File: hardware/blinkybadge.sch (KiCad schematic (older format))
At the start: 13 parts

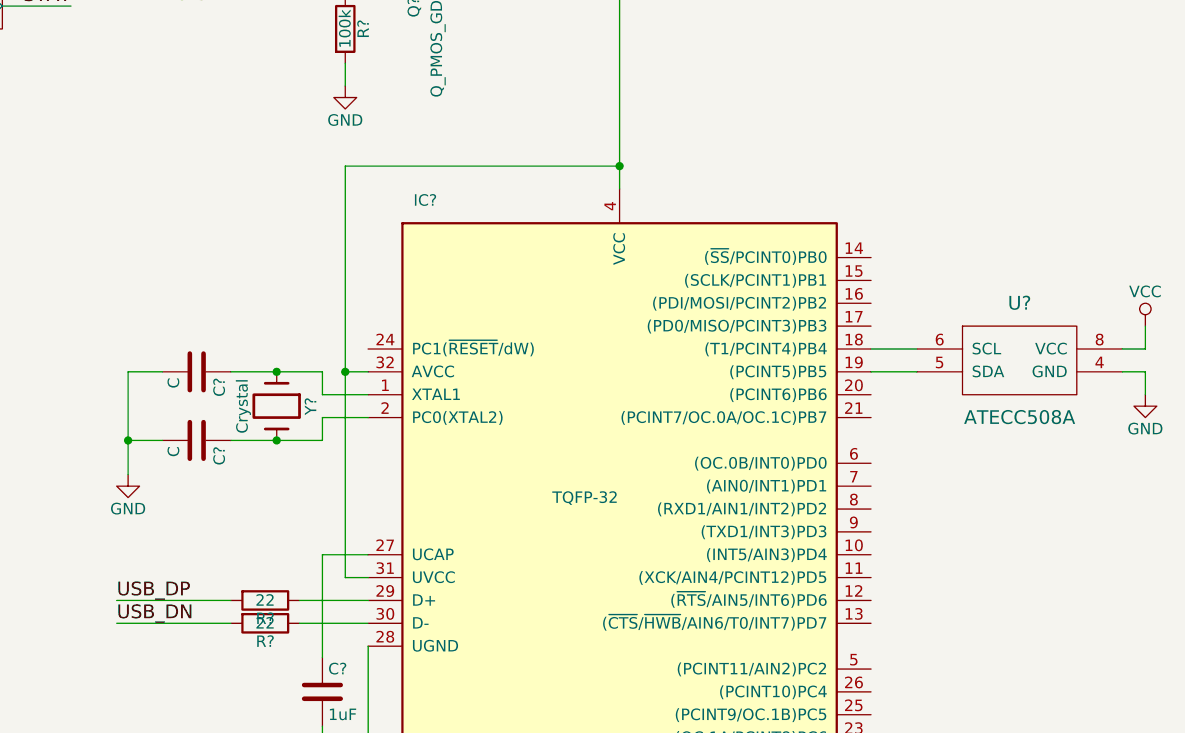
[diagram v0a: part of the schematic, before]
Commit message: Add LEDs
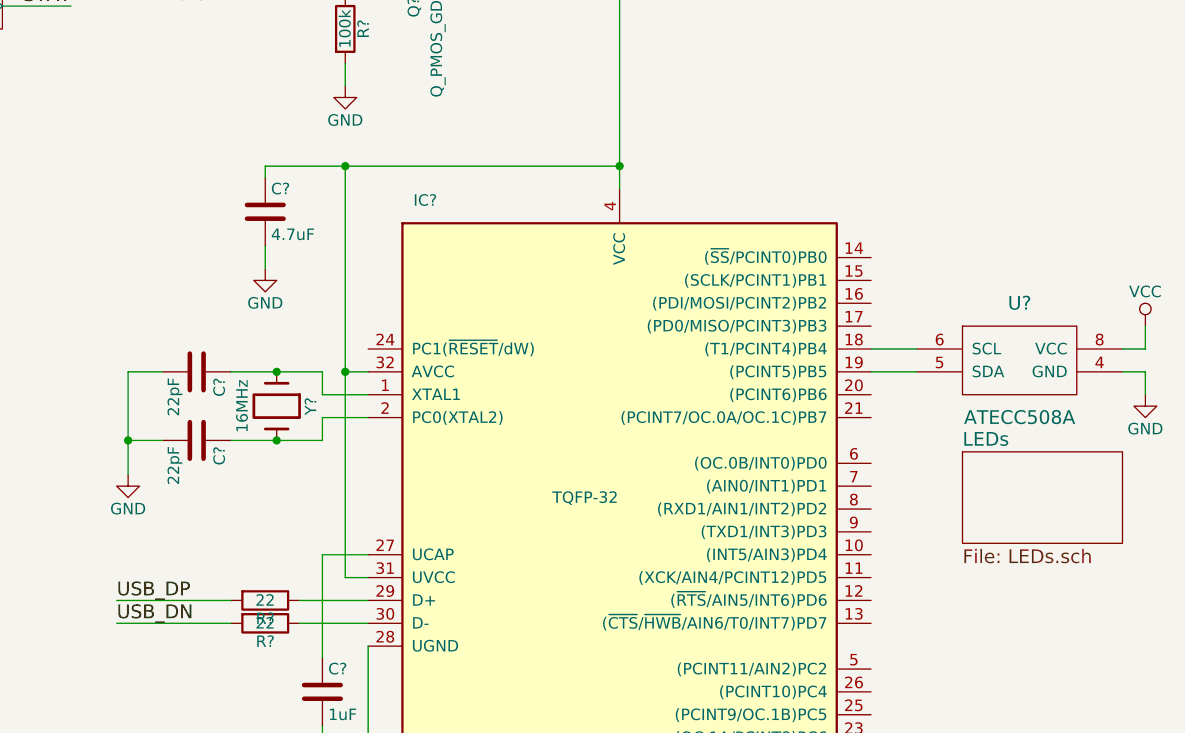
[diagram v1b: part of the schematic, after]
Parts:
- added C?: 4.7uF, symbol C
- C? (x2): value C -> 22pF
- Y?: value Crystal -> 16MHz
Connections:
- net GND: now also C?.2
- net VCC: now also C?.1
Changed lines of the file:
@@
 $Descr USLetter 11000 8500
 encoding utf-8
-Sheet 1 2
+Sheet 1 3
 Title "Crypto and Privacy Village 2016 Badge"
 Date ""
@@
 P 4200 3900
 F 0 "Y?" H 4200 4050 50  0000 C CNN
-F 1 "Crystal" H 4200 3750 50  0000 C CNN
+F 1 "16MHz" H 4200 3750 50  0000 C CNN
 F 2 "" H 4200 3900 50  0000 C CNN
 F 3 "" H 4200 3900 50  0000 C CNN
@@
 P 3850 3750
 F 0 "C?" H 3875 3850 50  0000 L CNN
-F 1 "C" H 3875 3650 50  0000 L CNN
+F 1 "22pF" H 3875 3650 50  0000 L CNN
 F 2 "" H 3888 3600 50  0000 C CNN
 F 3 "" H 3850 3750 50  0000 C CNN
@@
 P 3850 4050
 F 0 "C?" H 3875 4150 50  0000 L CNN
-F 1 "C" H 3875 3950 50  0000 L CNN
+F 1 "22pF" H 3875 3950 50  0000 L CNN
 F 2 "" H 3888 3900 50  0000 C CNN
 F 3 "" H 3850 4050 50  0000 C CNN
@@
 	8000 3650 8000 3550
 Wire Wire Line
-	5700 2850 4500 2850
+	4150 2850 5700 2850
 Wire Wire Line
 	4500 2850 4500 4650
@@
 	4500 4650 4600 4650
 Connection ~ 4500 3750
+$Comp
+L C C?
+U 1 1 577DC740
+P 4150 3050
+F 0 "C?" H 4175 3150 50  0000 L CNN
+F 1 "4.7uF" H 4175 2950 50  0000 L CNN
+F 2 "" H 4188 2900 50  0000 C CNN
+F 3 "" H 4150 3050 50  0000 C CNN
+	1    4150 3050
+	1    0    0    -1
+$EndComp
+Wire Wire Line
+	4150 2850 4150 2900
+Connection ~ 4500 2850
+$Comp
+L GND #PWR?
+U 1 1 577DC870
+P 4150 3300
+F 0 "#PWR?" H 4150 3050 50  0001 C CNN
+F 1 "GND" H 4150 3150 50  0000 C CNN
+F 2 "" H 4150 3300 50  0000 C CNN
+F 3 "" H 4150 3300 50  0000 C CNN
+	1    4150 3300
+	1    0    0    -1
+$EndComp
+Wire Wire Line
+	4150 3300 4150 3200
+$Sheet
+S 7200 4100 700  400
+U 577DCB06
+F0 "LEDs" 60
+F1 "LEDs.sch" 60
+$EndSheet
 $EndSCHEMATC

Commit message: Add annotations
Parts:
- gave numbers to parts that had none: 14
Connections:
- net LEDs/DIN: now reaches IC101.6 ((OC.0B/INT0)PD0)
- no-connect marks 1 -> 2

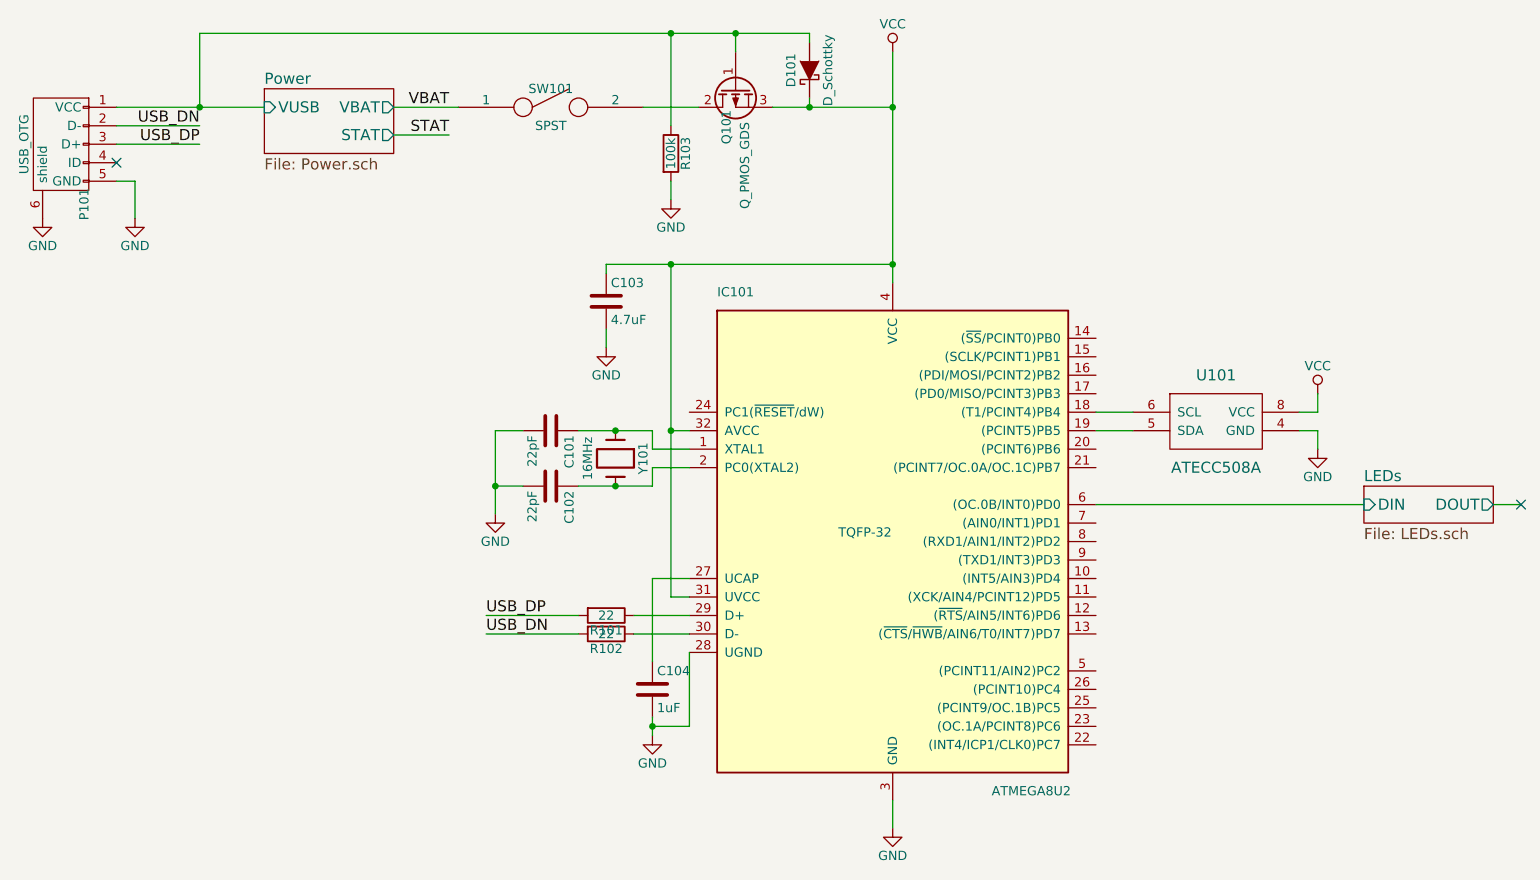
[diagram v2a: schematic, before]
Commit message: Add passives for touch sensor
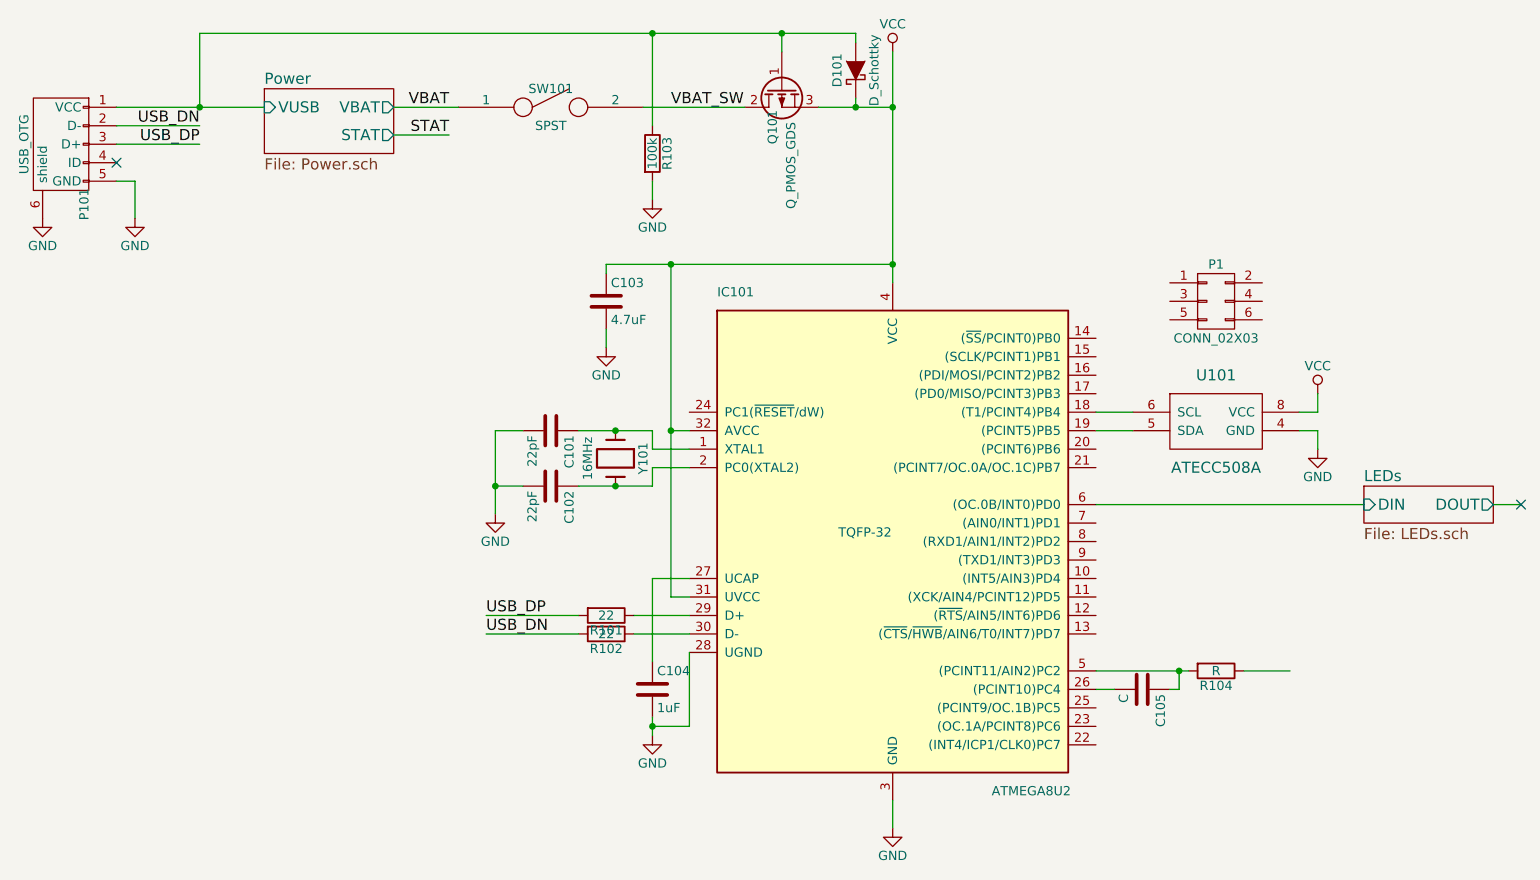
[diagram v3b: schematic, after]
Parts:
- added C105: C, symbol C
- added P1: CONN_02X03, symbol CONN_02X03
- added R104: R, symbol R
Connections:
- net VBAT_SW: now reaches Q101.2 (D), SW101.2
- net at IC101.26 ((PCINT10)PC4): now also C105.2
- net at IC101.5 ((PCINT11/AIN2)PC2): now also C105.1, R104.2
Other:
- moved on the sheet: D101, Q101, R103
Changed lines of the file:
@@
 L Q_PMOS_GDS Q101
 U 1 1 577C833B
-P 4850 1900
-F 0 "Q101" H 5150 1950 50  0000 R CNN
-F 1 "Q_PMOS_GDS" H 5500 1850 50  0000 R CNN
-F 2 "" H 5050 2000 50  0000 C CNN
-F 3 "" H 4850 1900 50  0000 C CNN
-	1    4850 1900
+P 5100 1900
+F 0 "Q101" H 5400 1950 50  0000 R CNN
+F 1 "Q_PMOS_GDS" H 5750 1850 50  0000 R CNN
+F 2 "" H 5300 2000 50  0000 C CNN
+F 3 "" H 5100 1900 50  0000 C CNN
+	1    5100 1900
 	0    -1   1    0
 $EndComp
@@
 L R R103
 U 1 1 577C870C
-P 4500 2250
-F 0 "R103" V 4580 2250 50  0000 C CNN
-F 1 "100k" V 4500 2250 50  0000 C CNN
-F 2 "" V 4430 2250 50  0000 C CNN
-F 3 "" H 4500 2250 50  0000 C CNN
-	1    4500 2250
-	1    0    0    -1
-$EndComp
-$Comp
-L GND #PWR106
+P 4400 2250
+F 0 "R103" V 4480 2250 50  0000 C CNN
+F 1 "100k" V 4400 2250 50  0000 C CNN
+F 2 "" V 4330 2250 50  0000 C CNN
+F 3 "" H 4400 2250 50  0000 C CNN
+	1    4400 2250
+	1    0    0    -1
+$EndComp
+$Comp
+L GND #PWR105
 U 1 1 577C87D2
-P 4500 2500
-F 0 "#PWR106" H 4500 2250 50  0001 C CNN
-F 1 "GND" H 4500 2350 50  0000 C CNN
-F 2 "" H 4500 2500 50  0000 C CNN
-F 3 "" H 4500 2500 50  0000 C CNN
-	1    4500 2500
+P 4400 2500
+F 0 "#PWR105" H 4400 2250 50  0001 C CNN
+F 1 "GND" H 4400 2350 50  0000 C CNN
+F 2 "" H 4400 2500 50  0000 C CNN
+F 3 "" H 4400 2500 50  0000 C CNN
+	1    4400 2500
 	1    0    0    -1
 $EndComp
@@
 L D_Schottky D101
 U 1 1 577C88F2
-P 5250 1800
-F 0 "D101" H 5250 1900 50  0000 C CNN
-F 1 "D_Schottky" H 5250 1700 50  0000 C CNN
-F 2 "" H 5250 1800 50  0000 C CNN
-F 3 "" H 5250 1800 50  0000 C CNN
-	1    5250 1800
+P 5500 1800
+F 0 "D101" H 5500 1900 50  0000 C CNN
+F 1 "D_Schottky" H 5500 1700 50  0000 C CNN
+F 2 "" H 5500 1800 50  0000 C CNN
+F 3 "" H 5500 1800 50  0000 C CNN
+	1    5500 1800
 	0    -1   -1   0
 $EndComp
@@
 $EndComp
 $Comp
-L GND #PWR105
+L GND #PWR106
 U 1 1 577C9628
 P 4400 5400
-F 0 "#PWR105" H 4400 5150 50  0001 C CNN
+F 0 "#PWR106" H 4400 5150 50  0001 C CNN
 F 1 "GND" H 4400 5250 50  0000 C CNN
 F 2 "" H 4400 5400 50  0000 C CNN
@@
 	5700 5750 5700 5900
 Wire Wire Line
-	4650 2000 4350 2000
-Wire Wire Line
-	4850 1600 4850 1700
-Wire Wire Line
-	1950 1600 5250 1600
+	4900 2000 4350 2000
+Wire Wire Line
+	5100 1600 5100 1700
+Wire Wire Line
+	1950 1600 5500 1600
 Wire Wire Line
 	1950 1600 1950 2000
 Connection ~ 1950 2000
 Wire Wire Line
-	4500 1600 4500 2100
-Connection ~ 4500 1600
-Wire Wire Line
-	4500 2400 4500 2500
-Connection ~ 4850 1600
-Wire Wire Line
-	5050 2000 5700 2000
+	4400 1600 4400 2100
+Connection ~ 4400 1600
+Wire Wire Line
+	4400 2400 4400 2500
+Connection ~ 5100 1600
+Wire Wire Line
+	5300 2000 5700 2000
 Wire Wire Line
 	5700 1700 5700 2950
-Connection ~ 5250 2000
-Wire Wire Line
-	5250 1600 5250 1650
-Wire Wire Line
-	5250 1950 5250 2000
+Connection ~ 5500 2000
+Wire Wire Line
+	5500 1600 5500 1650
+Wire Wire Line
+	5500 1950 5500 2000
 Wire Wire Line
 	3000 2150 3300 2150
@@
 	8950 4150 9100 4150
 NoConn ~ 9100 4150
+Text Label 4500 2000 0    60   ~ 0
+VBAT_SW
+$Comp
+L C C105
+U 1 1 577EF93B
+P 7050 5150
+F 0 "C105" H 7075 5250 50  0000 L CNN
+F 1 "C" H 7075 5050 50  0000 L CNN
+F 2 "" H 7088 5000 50  0000 C CNN
+F 3 "" H 7050 5150 50  0000 C CNN
+	1    7050 5150
+	0    1    1    0
+$EndComp
+$Comp
+L R R104
+U 1 1 577EF9C0
+P 7450 5050
+F 0 "R104" V 7530 5050 50  0000 C CNN
+F 1 "R" V 7450 5050 50  0000 C CNN
+F 2 "" V 7380 5050 50  0000 C CNN
+F 3 "" H 7450 5050 50  0000 C CNN
+	1    7450 5050
+	0    1    1    0
+$EndComp
+Wire Wire Line
+	6800 5050 7300 5050
+Wire Wire Line
+	6800 5150 6900 5150
+Wire Wire Line
+	7200 5150 7250 5150
+Wire Wire Line
+	7250 5150 7250 5050
+Connection ~ 7250 5050
+Wire Wire Line
+	7600 5050 7850 5050
+$Comp
+L CONN_02X03 P1
+U 1 1 577F2CCD
+P 7450 3050
+F 0 "P1" H 7450 3250 50  0000 C CNN
+F 1 "CONN_02X03" H 7450 2850 50  0000 C CNN
+F 2 "" H 7450 1850 50  0000 C CNN
+F 3 "" H 7450 1850 50  0000 C CNN
+	1    7450 3050
+	1    0    0    -1
+$EndComp
 $EndSCHEMATC

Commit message: Update footprints
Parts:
- C101, C102: value 22pF -> 18pF; footprint (none) -> Capacitors_SMD:C_0603
- C103, C104, C105: footprint (none) -> Capacitors_SMD:C_0603
- IC101: footprint TQFP-32 -> Housings_QFP:TQFP-32_7x7mm_Pitch0.8mm
- R101, R102, R103, R104: footprint (none) -> Resistors_SMD:R_0603
- U101: footprint (none) -> Housings_SOIC:SOIC-8_3.9x4.9mm_Pitch1.27mm
- Y101: footprint (none) -> Crystals:Crystal_HC49-SD_SMD
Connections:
- net GND: now also P1.6 (P6)
- net VCC: now also P1.2 (P2)
- net at IC101.15 ((SCLK/PCINT1)PB1): now also P1.3 (P3)
- net at IC101.16 ((PDI/MOSI/PCINT2)PB2): now also P1.4 (P4)
- net at IC101.17 ((PD0/MISO/PCINT3)PB3): now also P1.1 (P1)
- net at IC101.24 (PC1(~RESET~/dW)): now also P1.5 (P5)
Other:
- moved on the sheet: P1

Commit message: Update some footprint assignments
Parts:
- D101: footprint (none) -> Diodes_SMD:SOD-323
- P101: footprint (none) -> Connect:USB_Micro-B
- Q101: footprint (none) -> TO_SOT_Packages_SMD:SOT-23
- renumbered P1 to P102
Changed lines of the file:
@@
 F 0 "P101" H 1525 2075 50  0000 C CNN
 F 1 "USB_OTG" H 1200 2400 50  0000 C CNN
-F 2 "" V 1150 2100 50  0001 C CNN
+F 2 "Connect:USB_Micro-B" V 1150 2100 50  0001 C CNN
 F 3 "" V 1150 2100 50  0000 C CNN
 	1    1200 2200
@@
 F 0 "Q101" H 5400 1950 50  0000 R CNN
 F 1 "Q_PMOS_GDS" H 5750 1850 50  0000 R CNN
-F 2 "" H 5300 2000 50  0001 C CNN
+F 2 "TO_SOT_Packages_SMD:SOT-23" H 5300 2000 50  0001 C CNN
 F 3 "" H 5100 1900 50  0000 C CNN
 	1    5100 1900
@@
 F 0 "D101" H 5500 1900 50  0000 C CNN
 F 1 "D_Schottky" H 5500 1700 50  0000 C CNN
-F 2 "" H 5500 1800 50  0001 C CNN
+F 2 "Diodes_SMD:SOD-323" H 5500 1800 50  0001 C CNN
 F 3 "" H 5500 1800 50  0000 C CNN
 	1    5500 1800
@@
 $EndComp
 $Comp
-L CONN_02X03 P1
+L CONN_02X03 P102
 U 1 1 577F2CCD
 P 7450 2650
-F 0 "P1" H 7450 2850 50  0000 C CNN
+F 0 "P102" H 7450 2850 50  0000 C CNN
 F 1 "CONN_02X03" H 7450 2450 50  0000 C CNN
 F 2 "" H 7450 1450 50  0001 C CNN

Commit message: Update some footprint assignments
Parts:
- P101: footprint Connect:USB_Micro-B -> lib:USB_Micro-B-cpv
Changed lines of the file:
@@
 F 0 "P101" H 1525 2075 50  0000 C CNN
 F 1 "USB_OTG" H 1200 2400 50  0000 C CNN
-F 2 "Connect:USB_Micro-B" V 1150 2100 50  0001 C CNN
+F 2 "lib:USB_Micro-B-cpv" V 1150 2100 50  0001 C CNN
 F 3 "" V 1150 2100 50  0000 C CNN
 	1    1200 2200

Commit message: Begin layout work
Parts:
- added C106: 1uF, Capacitors_SMD:C_0603, symbol C
- added W1: RXD, Measurement_Points:Measurement_Point_Round-SMD-Pad_Small, symbol TEST_1P
- added W2: TXD, Measurement_Points:Measurement_Point_Round-SMD-Pad_Small, symbol TEST_1P
- added W3: CAP_SENSE_BUTTON, Measurement_Points:Measurement_Point_Round-SMD-Pad_Small, symbol TEST_1P
- SW101: footprint (none) -> lib:DPDT_SMD
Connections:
- net GND: now also C106.2
- net VCC: now also C106.1
- net at IC101.8 ((RXD1/AIN1/INT2)PD2): now also W1.1
- net at IC101.9 ((TXD1/INT3)PD3): now also W2.1
- net at R104.1: now also W3.1
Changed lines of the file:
@@
 F 0 "SW101" H 3850 2100 50  0000 C CNN
 F 1 "SPST" H 3850 1900 50  0000 C CNN
-F 2 "" H 3850 2000 50  0001 C CNN
+F 2 "lib:DPDT_SMD" H 3850 2000 50  0001 C CNN
 F 3 "" H 3850 2000 50  0000 C CNN
 	1    3850 2000
@@
 	1    0    0    -1
 $EndComp
+$Comp
+L TEST_1P W1
+U 1 1 5780255A
+P 6950 4350
+F 0 "W1" H 6950 4620 50  0000 C CNN
+F 1 "RXD" H 6950 4550 50  0000 C CNN
+F 2 "Measurement_Points:Measurement_Point_Round-SMD-Pad_Small" H 7150 4350 50  0001 C CNN
+F 3 "" H 7150 4350 50  0000 C CNN
+	1    6950 4350
+	0    1    1    0
+$EndComp
+$Comp
+L TEST_1P W2
+U 1 1 578025E3
+P 6950 4450
+F 0 "W2" H 6950 4720 50  0000 C CNN
+F 1 "TXD" H 6950 4650 50  0000 C CNN
+F 2 "Measurement_Points:Measurement_Point_Round-SMD-Pad_Small" H 7150 4450 50  0001 C CNN
+F 3 "" H 7150 4450 50  0000 C CNN
+	1    6950 4450
+	0    1    1    0
+$EndComp
+Wire Wire Line
+	6950 4350 6800 4350
+Wire Wire Line
+	6800 4450 6950 4450
+$Comp
+L TEST_1P W3
+U 1 1 57805F3E
+P 7850 5050
+F 0 "W3" H 7850 5320 50  0000 C CNN
+F 1 "CAP_SENSE_BUTTON" H 7850 5250 50  0000 C CNN
+F 2 "Measurement_Points:Measurement_Point_Round-SMD-Pad_Small" H 8050 5050 50  0001 C CNN
+F 3 "" H 8050 5050 50  0000 C CNN
+	1    7850 5050
+	1    0    0    -1
+$EndComp
+$Comp
+L C C106
+U 1 1 57802CCD
+P 8200 3700
+F 0 "C106" H 8225 3800 50  0000 L CNN
+F 1 "1uF" H 8225 3600 50  0000 L CNN
+F 2 "Capacitors_SMD:C_0603" H 8238 3550 50  0001 C CNN
+F 3 "" H 8200 3700 50  0000 C CNN
+	1    8200 3700
+	1    0    0    -1
+$EndComp
+Wire Wire Line
+	8000 3550 8200 3550
+Wire Wire Line
+	8000 3850 8200 3850
 $EndSCHEMATC
